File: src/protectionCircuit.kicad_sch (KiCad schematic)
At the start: 20 parts, among them M1 CSD19534Q5A, M2 CSD19534Q5A, U1 LM74910QRGERQ1

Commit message: Test Updates - tst
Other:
- note added: "Test Update Here Too"
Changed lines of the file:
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@@
 	(generator_version "10.0")
 	(paper "A")
+	(text "Test Update Here Too"
+		(exclude_from_sim no)
+		(at 126.746 36.576 0)
+		(effects
+			(font
+				(size 2.54 2.54)
+			)
+		)
+	)
 	(junction
 		(at 208.28 60.96)

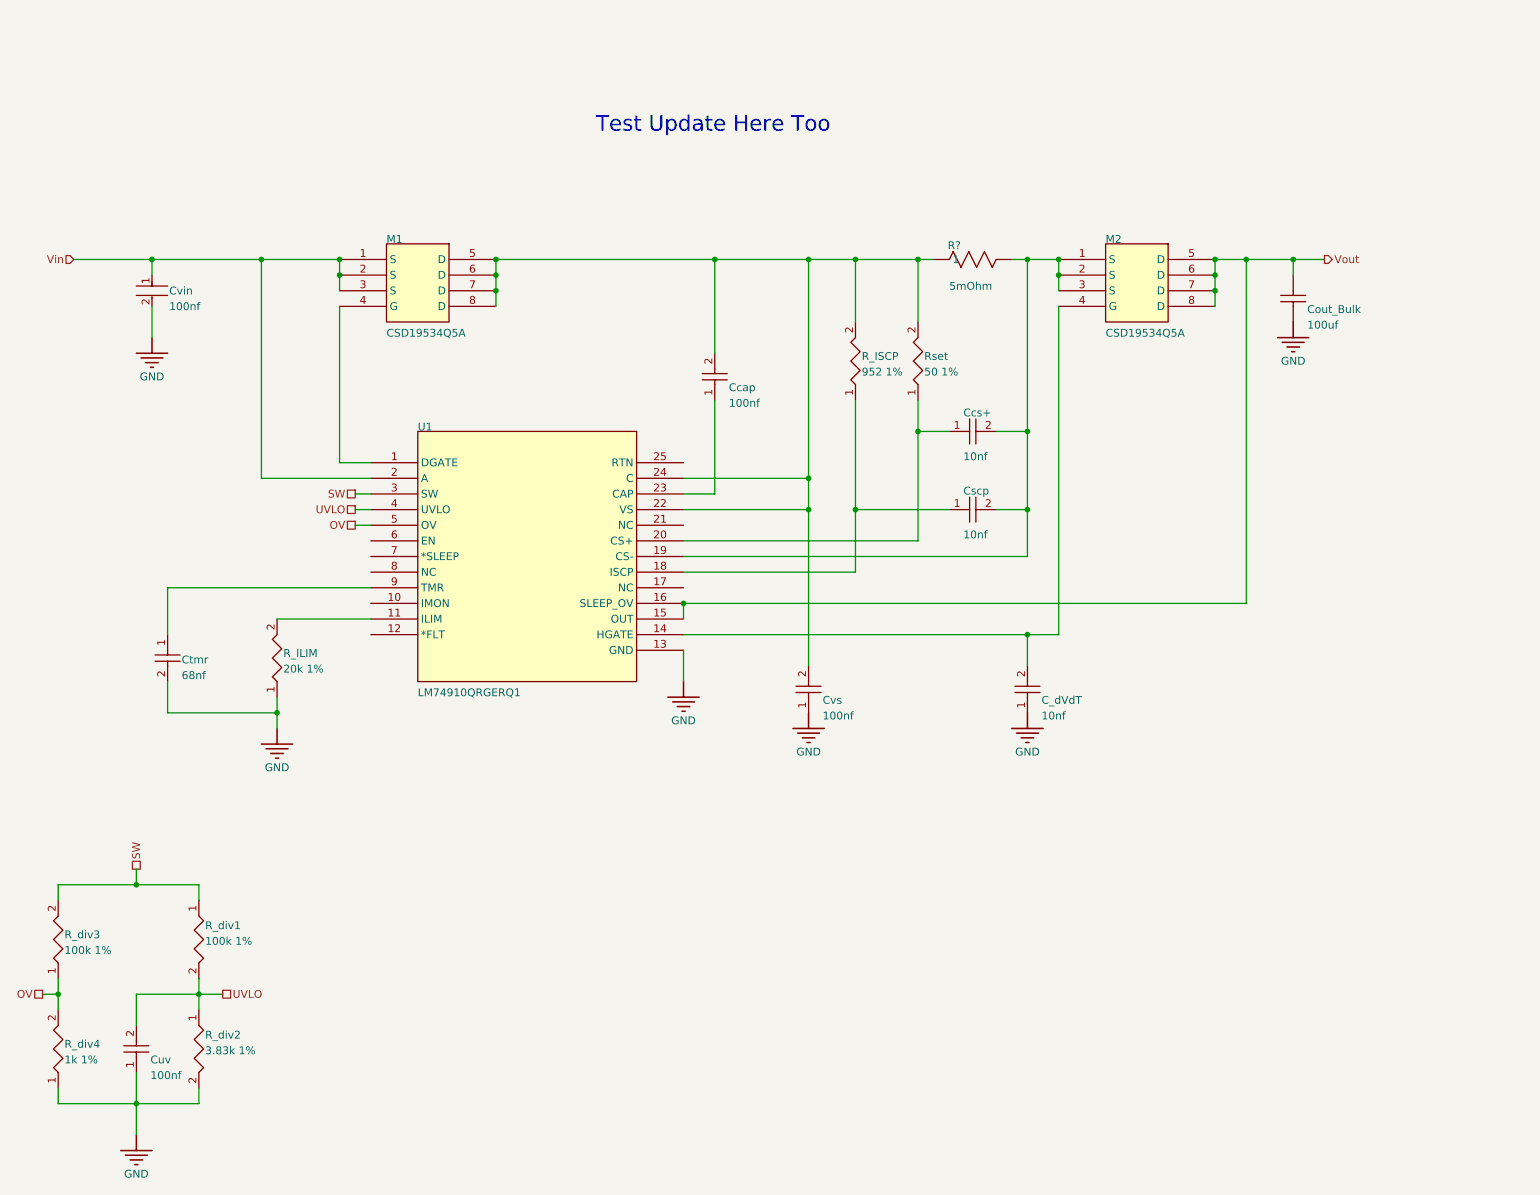
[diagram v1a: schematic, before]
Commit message: Updated majority of passive components to KiCad format
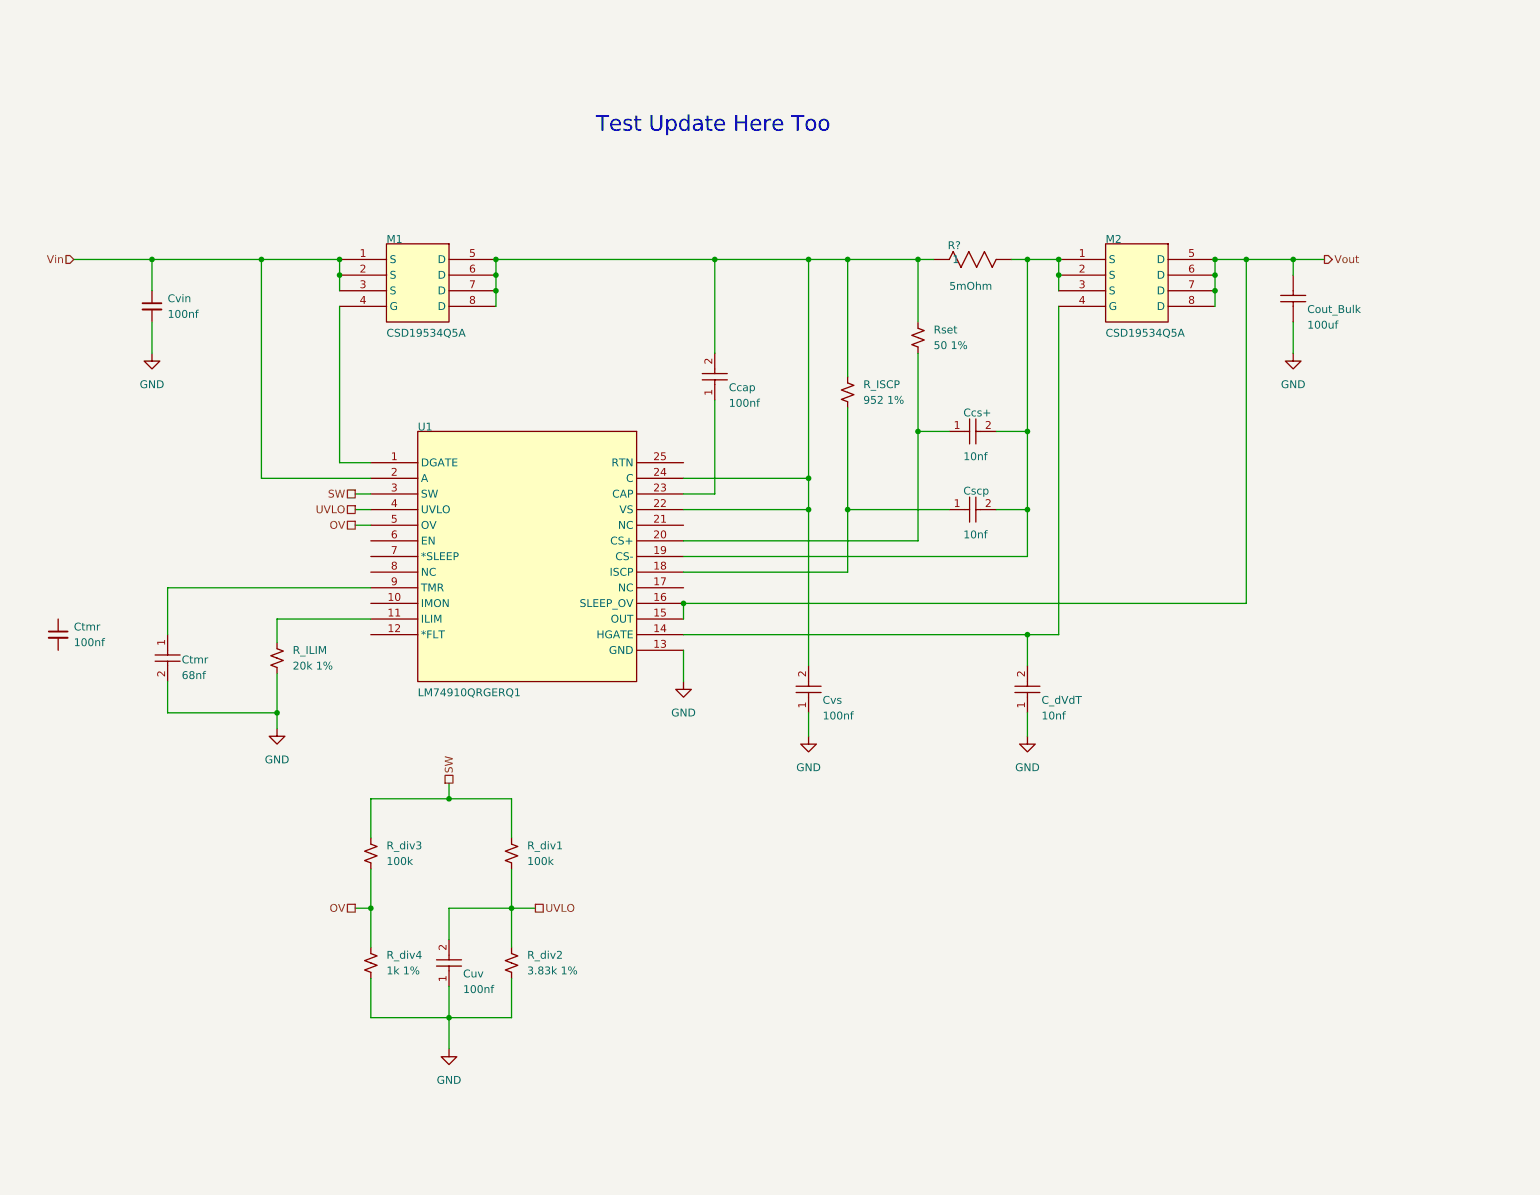
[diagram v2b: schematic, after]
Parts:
- removed Cvin: 100nf, powerDristributionBoard-import-fps:FP-CNA6P-MFG, symbol Altium Content Vault:b4654b650e69147ec39a6b967a45e02
- removed R_ILIM, R_ISCP, R_div1, R_div2, R_div3, R_div4, Rset: Resistor 22R +/-1% 0603 100 mW, powerDristributionBoard-import-fps:RESC1609X50X30ML08T20, symbol Autonomous Vehicle Lab:RES-2
- added Ctmr: 100nf, Capacitor_SMD:C_0603_1608Metric, symbol Device:C_Small
- added Cvin: 100nf, Capacitor_SMD:C_1210_3225Metric, symbol Device:C_Small
- added R_ILIM: 20k 1%, Resistor_SMD:R_0603_1608Metric, symbol Device:R_Small_US
- added R_ISCP: 952 1%, Resistor_SMD:R_0603_1608Metric, symbol Device:R_Small_US
- added R_div1, R_div3: 100k, Resistor_SMD:R_0603_1608Metric, symbol Device:R_Small_US
- added R_div2: 3.83k 1%, Resistor_SMD:R_0603_1608Metric, symbol Device:R_Small_US
- added R_div4: 1k 1%, Resistor_SMD:R_0603_1608Metric, symbol Device:R_Small_US
- added Rset: 50 1%, Resistor_SMD:R_0603_1608Metric, symbol Device:R_Small_US
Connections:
- net GND: now also Cvin.2, R_ILIM.2, R_div2.2, R_div4.2
- net OV: now also R_div3.2, R_div4.1
- net SW: now also R_div1.1, R_div3.1
- net UVLO: now also R_div1.2, R_div2.1
- net Vin: now also Cvin.1
- net at Ccap.2, Cvs.2, M1.5 (D)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: now also R_ISCP.1, Rset.1
- net at Cscp.1, U1.18 (ISCP): now also R_ISCP.2
- net at Ccs+.1, U1.20 (CS+): now also Rset.2
- net at U1.11 (ILIM): now also R_ILIM.1
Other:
- moved on the sheet: Cuv

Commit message: Test push protection circuit
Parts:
- removed Ctmr: Capacitor 470nF +/-20% 25V 0603, powerDristributionBoard-import-fps:CAPC0603(1608)100_L, symbol Autonomous Vehicle Lab:CAP-NP-2
- added Ctmr1, Ctmr2, Ctmr3, Ctmr4: 68nf, Capacitor_SMD:C_0603_1608Metric, symbol Device:C_Small
- Ctmr: value 100nf -> 68nf
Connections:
- net GND: now also Ctmr.2
- net at U1.9 (TMR): now also Ctmr.1
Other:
- moved on the sheet: Ctmr

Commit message: Test Push again
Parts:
- removed Ctmr1, Ctmr2, Ctmr3, Ctmr4: 68nf, Capacitor_SMD:C_0603_1608Metric, symbol Device:C_Small
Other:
- note removed: "Test Update Here Too"

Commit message: Test Push again
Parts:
- added Ctmr1, Ctmr2, Ctmr3, Ctmr4, Ctmr5: 68nf, Capacitor_SMD:C_0603_1608Metric, symbol Device:C_Small

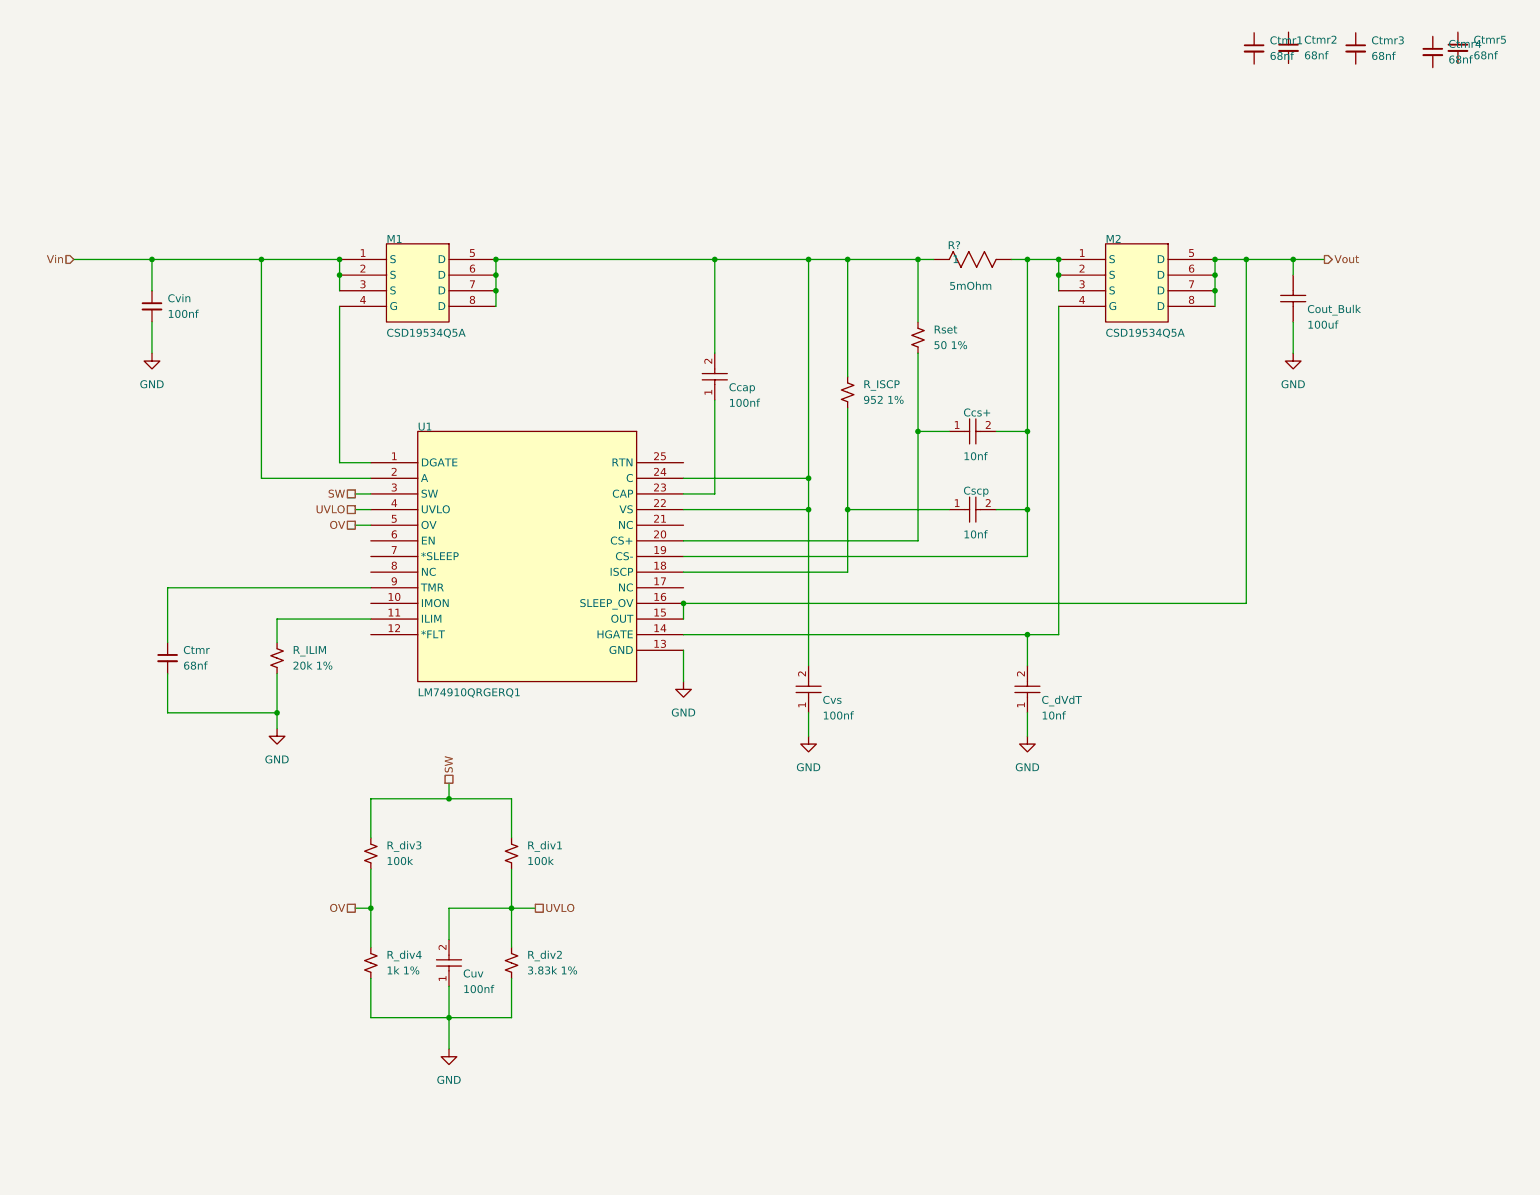
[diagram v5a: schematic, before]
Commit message: Updated all passive components to KiCad version
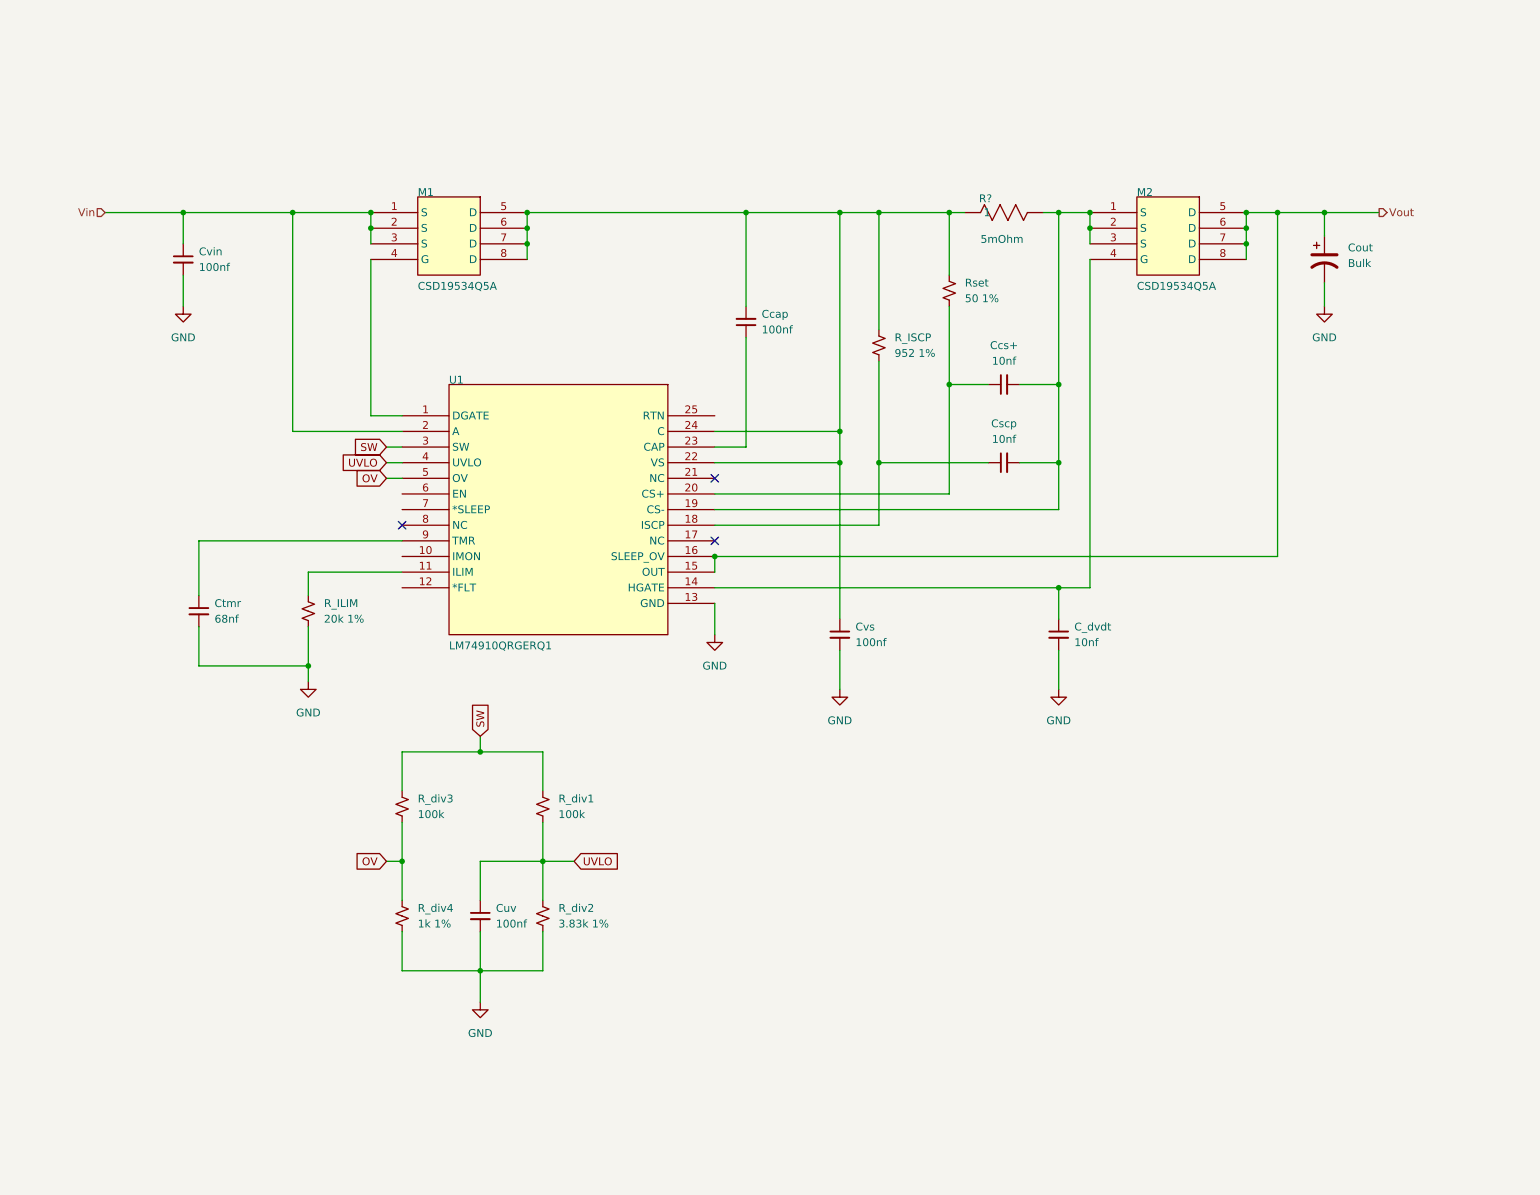
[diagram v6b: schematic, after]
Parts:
- removed C_dVdT, Ccap, Ccs+, Cscp, Cuv, Cvs: Capacitor 470nF +/-20% 25V 0603, powerDristributionBoard-import-fps:CAPC0603(1608)100_L, symbol Autonomous Vehicle Lab:CAP-NP-2
- removed Cout_Bulk: Capacitor, symbol Simulation Generic Components:Capacitor
- removed Ctmr1, Ctmr2, Ctmr3, Ctmr4, Ctmr5: 68nf, Capacitor_SMD:C_0603_1608Metric, symbol Device:C_Small
- added C_dvdt, Ccs+, Cscp: 10nf, Capacitor_SMD:C_0603_1608Metric, symbol Device:C_Small
- added Ccap, Cuv, Cvs: 100nf, Capacitor_SMD:C_0603_1608Metric, symbol Device:C_Small
- added Cout: Bulk, symbol Device:C_Polarized_US
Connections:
- net GND: now also C_dvdt.2, Cout.2, Cuv.2, Cvs.2
- net UVLO: now also Cuv.1
- net Vout: now also Cout.1
- net at M2.4 (G), U1.14 (HGATE): now also C_dvdt.1
- net at M1.5 (D), M1.6 (D), M1.7 (D)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: now also Ccap.2, Cvs.1
- net at M2.1 (S), M2.2 (S), M2.3 (S)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: now also Ccs+.2, Cscp.2
- net at R_ISCP.2, U1.18 (ISCP): now also Cscp.1
- net at Rset.2, U1.20 (CS+): now also Ccs+.1
- net at U1.23 (CAP): now also Ccap.1
- no-connect marks 0 -> 3
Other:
- moved on the sheet: Ctmr, Cvin, M1, M2, R?, R_ILIM, R_ISCP, R_div1, R_div2, R_div3, R_div4, Rset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
